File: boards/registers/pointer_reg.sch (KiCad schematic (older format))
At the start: 42 parts, among them U10 MC74ACT161DG, U11 SN74ACT244PW, U12 SN74ACT244PW, U13 MC74ACT161DG, U14 MC74ACT161DG, U15 SN74ACT244PW, U16 SN74ACT244PW, U9 MC74ACT161DG

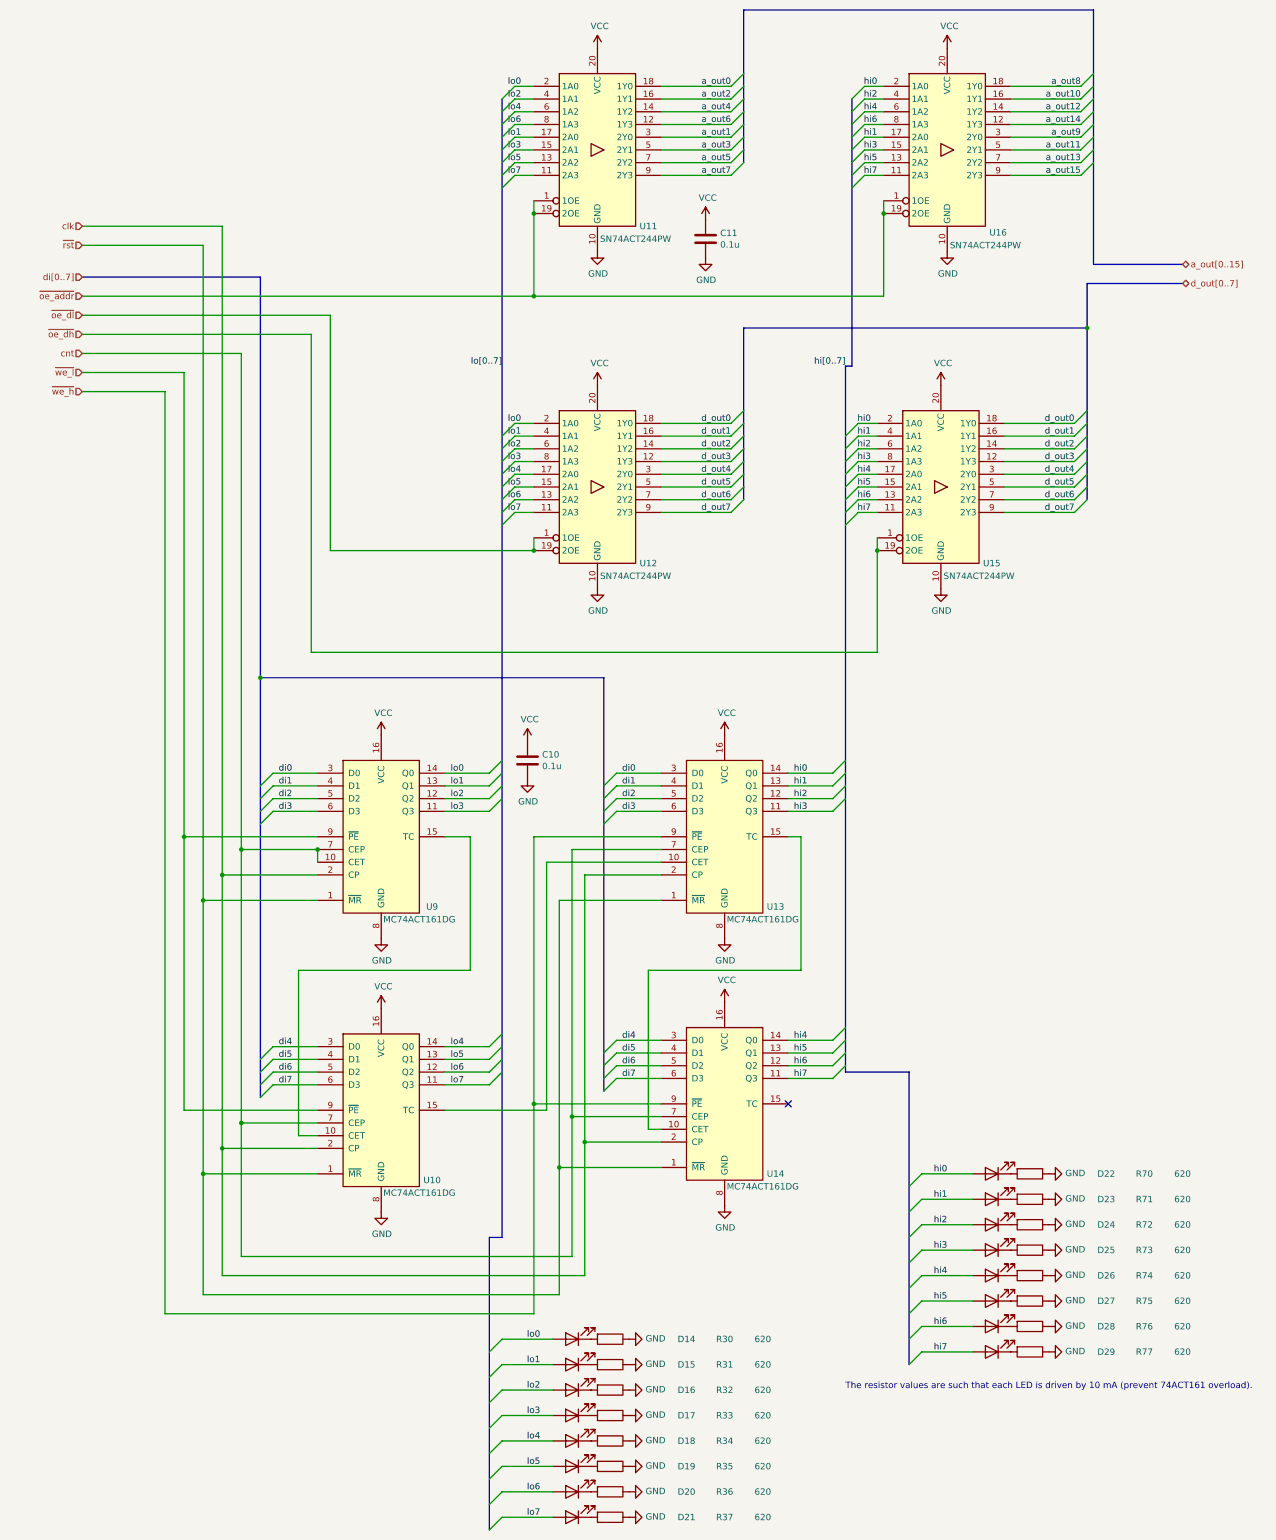
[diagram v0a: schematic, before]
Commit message: Registers: new clock and reset
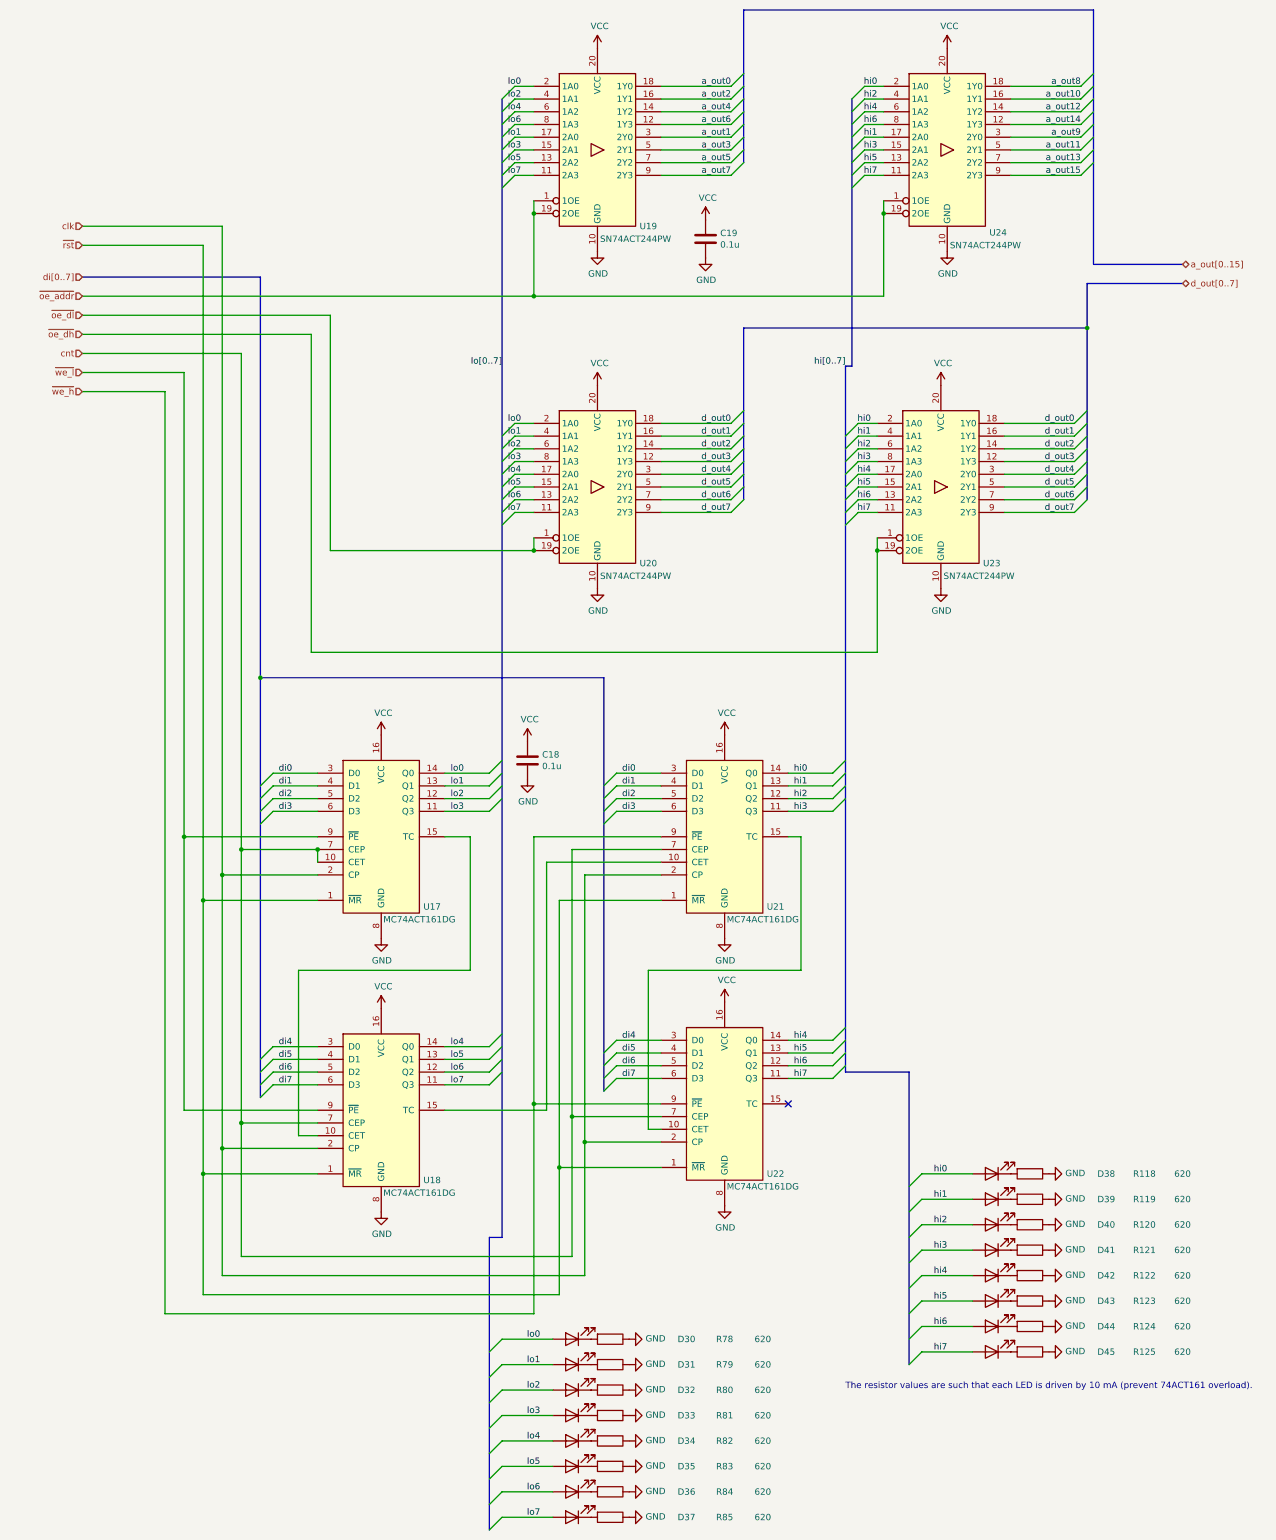
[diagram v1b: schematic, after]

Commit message: Registers: more decoupling capacitors
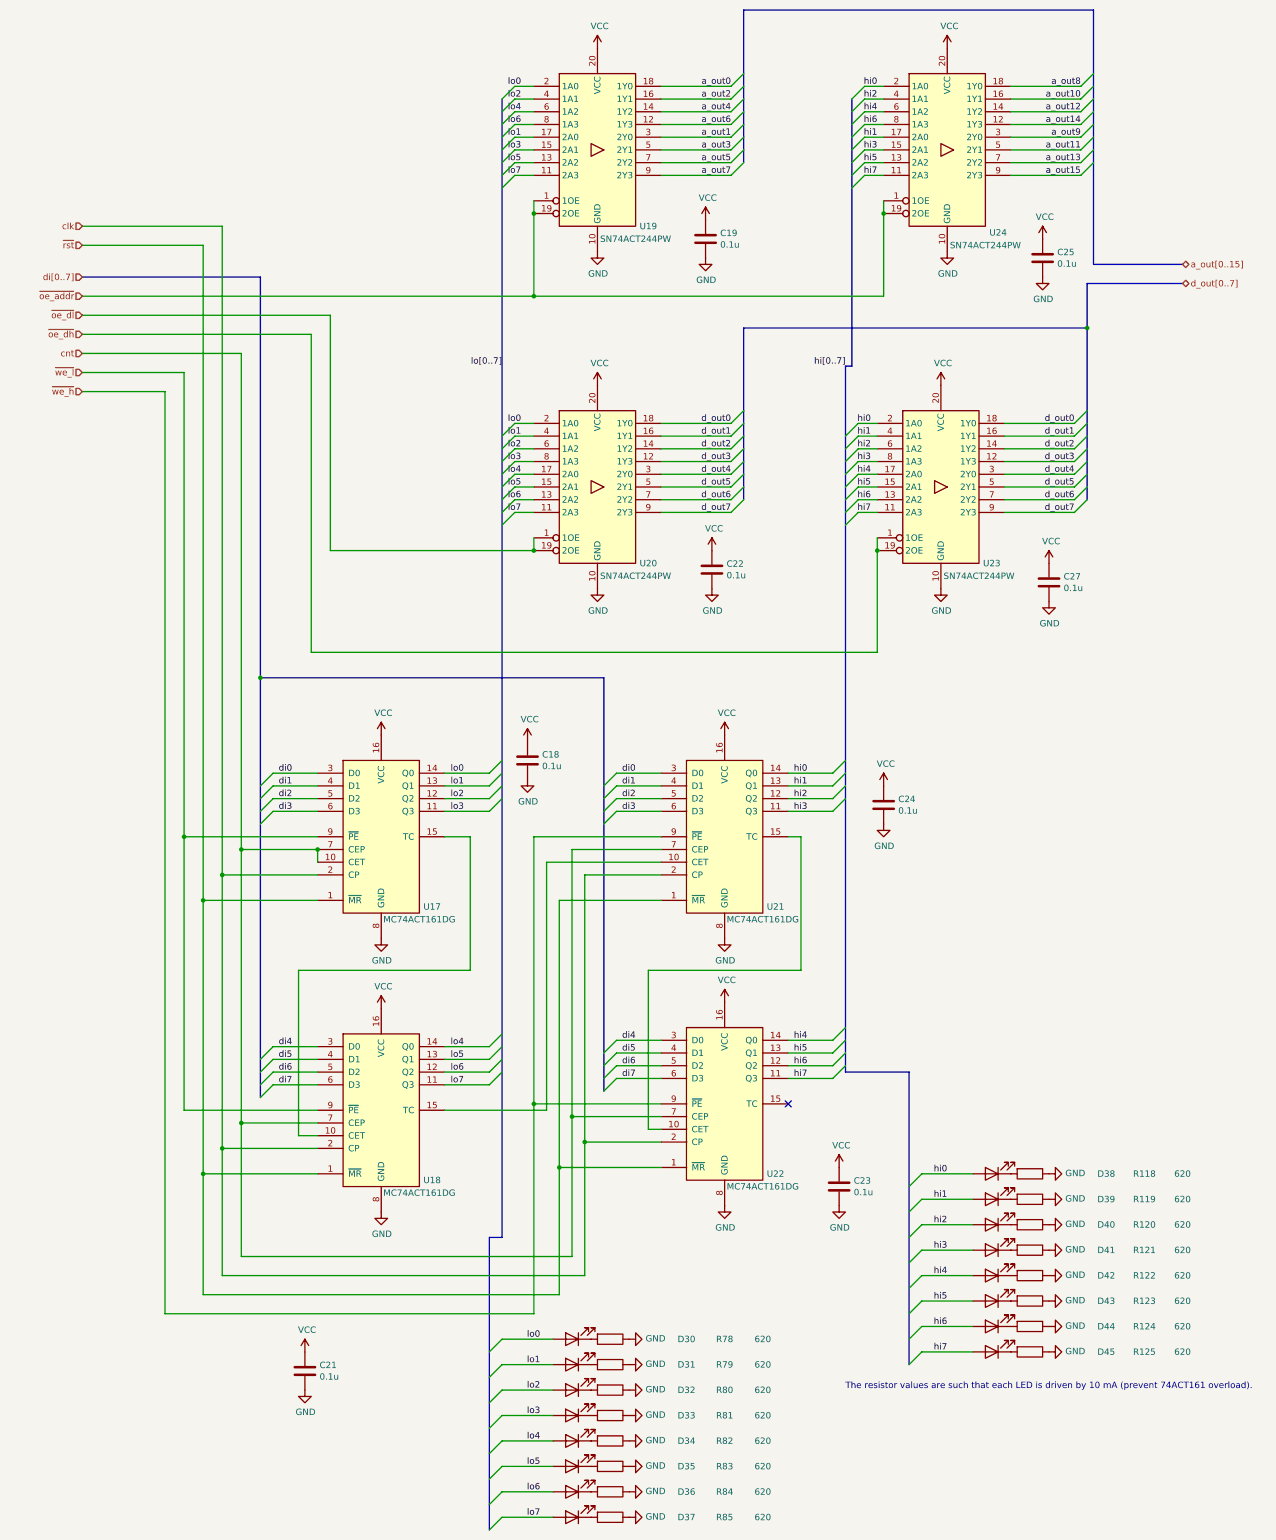
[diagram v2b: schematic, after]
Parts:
- added C13, C14, C15, C16, C17, C20: 0.1u, Capacitor_SMD:C_0805_2012Metric, symbol Device:C
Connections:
- net GND: now also C13.2, C14.2, C15.2, C16.2, C17.2, C20.2
- net VCC: now also C13.1, C14.1, C15.1, C16.1, C17.1, C20.1

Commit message: Registers: change logic family to HC and LV-A
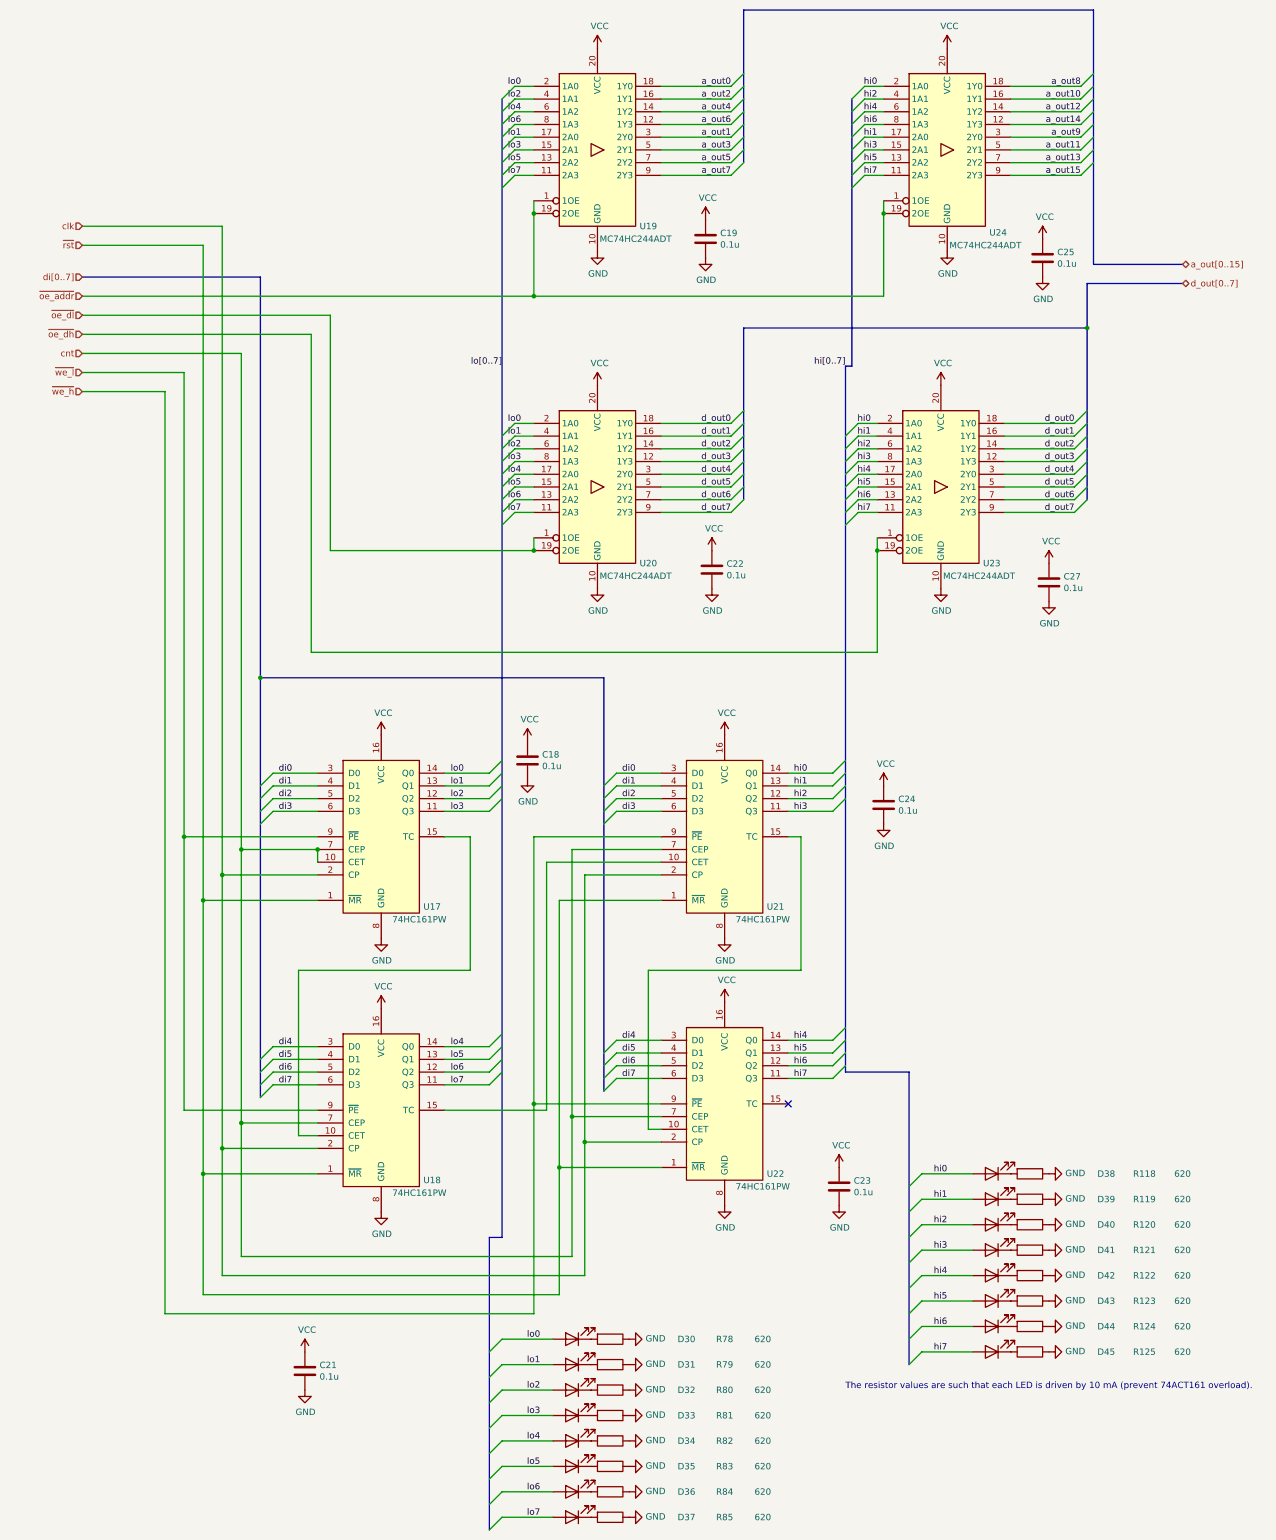
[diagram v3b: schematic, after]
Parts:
- U10, U13, U14, U9: value MC74ACT161DG -> 74HC161PW; footprint Package_SO:SOIC-16_3.9x9.9mm_P1.27mm -> Package_SO:TSSOP-16_4.4x5mm_P0.65mm
- U11, U12, U15, U16: value SN74ACT244PW -> MC74HC244ADT
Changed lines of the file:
@@
 AR Path="/5E0666E8/5E5C90D9/5E067470" Ref="U19"  Part="1"
 F 0 "U19" H 5950 3250 50  0000 C CNN
-F 1 "SN74ACT244PW" H 5850 3150 50  0000 C CNN
+F 1 "MC74HC244ADT" H 5850 3150 50  0000 C CNN
 F 2 "Package_SO:TSSOP-20_4.4x6.5mm_P0.65mm" H 5550 3850 50  0001 C CNN
-F 3 "https://assets.nexperia.com/documents/data-sheet/74HC_HCT244.pdf" H 5550 3850 50  0001 C CNN
+F 3 "http://www.farnell.com/datasheets/1878565.pdf" H 5550 3850 50  0001 C CNN
 	1    5550 3850
 	1    0    0    -1
@@
 AR Path="/5E0666E8/5E5C90D9/5E06F6F1" Ref="U24"  Part="1"
 F 0 "U24" H 8700 3200 50  0000 C CNN
-F 1 "SN74ACT244PW" H 8600 3100 50  0000 C CNN
+F 1 "MC74HC244ADT" H 8600 3100 50  0000 C CNN
 F 2 "Package_SO:TSSOP-20_4.4x6.5mm_P0.65mm" H 8300 3850 50  0001 C CNN
-F 3 "https://assets.nexperia.com/documents/data-sheet/74HC_HCT244.pdf" H 8300 3850 50  0001 C CNN
+F 3 "http://www.farnell.com/datasheets/1878565.pdf" H 8300 3850 50  0001 C CNN
 	1    8300 3850
 	1    0    0    -1
@@
 AR Path="/5E0666E8/5E5C90D9/5E07142A" Ref="U20"  Part="1"
 F 0 "U20" H 5950 5900 50  0000 C CNN
-F 1 "SN74ACT244PW" H 5850 5800 50  0000 C CNN
+F 1 "MC74HC244ADT" H 5850 5800 50  0000 C CNN
 F 2 "Package_SO:TSSOP-20_4.4x6.5mm_P0.65mm" H 5550 6500 50  0001 C CNN
-F 3 "https://assets.nexperia.com/documents/data-sheet/74HC_HCT244.pdf" H 5550 6500 50  0001 C CNN
+F 3 "http://www.farnell.com/datasheets/1878565.pdf" H 5550 6500 50  0001 C CNN
 	1    5550 6500
 	1    0    0    -1
@@
 AR Path="/5E0666E8/5E5C90D9/5E072984" Ref="U23"  Part="1"
 F 0 "U23" H 8650 5900 50  0000 C CNN
-F 1 "SN74ACT244PW" H 8550 5800 50  0000 C CNN
+F 1 "MC74HC244ADT" H 8550 5800 50  0000 C CNN
 F 2 "Package_SO:TSSOP-20_4.4x6.5mm_P0.65mm" H 8250 6500 50  0001 C CNN
-F 3 "https://assets.nexperia.com/documents/data-sheet/74HC_HCT244.pdf" H 8250 6500 50  0001 C CNN
+F 3 "http://www.farnell.com/datasheets/1878565.pdf" H 8250 6500 50  0001 C CNN
 	1    8250 6500
 	1    0    0    -1
@@
 AR Path="/5E0666E8/5E5C90D9/5E0E2189" Ref="U17"  Part="1"
 F 0 "U17" H 4250 8700 50  0000 C CNN
-F 1 "MC74ACT161DG" H 4150 8600 50  0000 C CNN
-F 2 "Package_SO:SOIC-16_3.9x9.9mm_P1.27mm" H 3850 9250 50  0001 C CNN
-F 3 "http://www.ti.com/lit/gpn/sn74LS161" H 3850 9250 50  0001 C CNN
+F 1 "74HC161PW" H 4150 8600 50  0000 C CNN
+F 2 "Package_SO:TSSOP-16_4.4x5mm_P0.65mm" H 3850 9250 50  0001 C CNN
+F 3 "http://www.farnell.com/datasheets/308767.pdf" H 3850 9250 50  0001 C CNN
 	1    3850 9250
 	1    0    0    -1
@@
 AR Path="/5E0666E8/5E5C90D9/5E0E857B" Ref="U18"  Part="1"
 F 0 "U18" H 4250 10850 50  0000 C CNN
-F 1 "MC74ACT161DG" H 4150 10750 50  0000 C CNN
-F 2 "Package_SO:SOIC-16_3.9x9.9mm_P1.27mm" H 3850 11400 50  0001 C CNN
-F 3 "http://www.ti.com/lit/gpn/sn74LS161" H 3850 11400 50  0001 C CNN
+F 1 "74HC161PW" H 4150 10750 50  0000 C CNN
+F 2 "Package_SO:TSSOP-16_4.4x5mm_P0.65mm" H 3850 11400 50  0001 C CNN
+F 3 "http://www.farnell.com/datasheets/308767.pdf" H 3850 11400 50  0001 C CNN
 	1    3850 11400
 	1    0    0    -1
@@
 AR Path="/5E0666E8/5E5C90D9/5E0E941D" Ref="U21"  Part="1"
 F 0 "U21" H 6950 8700 50  0000 C CNN
-F 1 "MC74ACT161DG" H 6850 8600 50  0000 C CNN
-F 2 "Package_SO:SOIC-16_3.9x9.9mm_P1.27mm" H 6550 9250 50  0001 C CNN
-F 3 "http://www.ti.com/lit/gpn/sn74LS161" H 6550 9250 50  0001 C CNN
+F 1 "74HC161PW" H 6850 8600 50  0000 C CNN
+F 2 "Package_SO:TSSOP-16_4.4x5mm_P0.65mm" H 6550 9250 50  0001 C CNN
+F 3 "http://www.farnell.com/datasheets/308767.pdf" H 6550 9250 50  0001 C CNN
 	1    6550 9250
 	1    0    0    -1
@@
 AR Path="/5E0666E8/5E5C90D9/5E0EB83E" Ref="U22"  Part="1"
 F 0 "U22" H 6950 10800 50  0000 C CNN
-F 1 "MC74ACT161DG" H 6850 10700 50  0000 C CNN
-F 2 "Package_SO:SOIC-16_3.9x9.9mm_P1.27mm" H 6550 11350 50  0001 C CNN
-F 3 "http://www.ti.com/lit/gpn/sn74LS161" H 6550 11350 50  0001 C CNN
+F 1 "74HC161PW" H 6850 10700 50  0000 C CNN
+F 2 "Package_SO:TSSOP-16_4.4x5mm_P0.65mm" H 6550 11350 50  0001 C CNN
+F 3 "http://www.farnell.com/datasheets/308767.pdf" H 6550 11350 50  0001 C CNN
 	1    6550 11350
 	1    0    0    -1
